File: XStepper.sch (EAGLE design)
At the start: 74 parts, among them Q2 16 MHZ

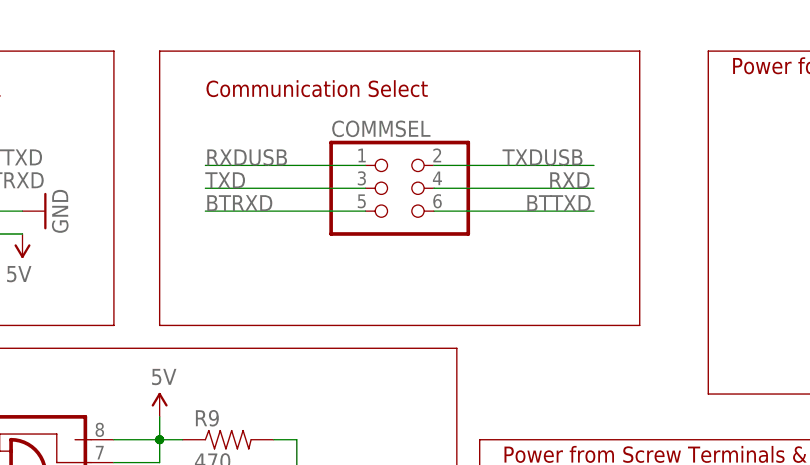
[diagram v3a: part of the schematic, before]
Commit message: - Bugfix COMSERIAL
change pins on comserial block
remove some unused files
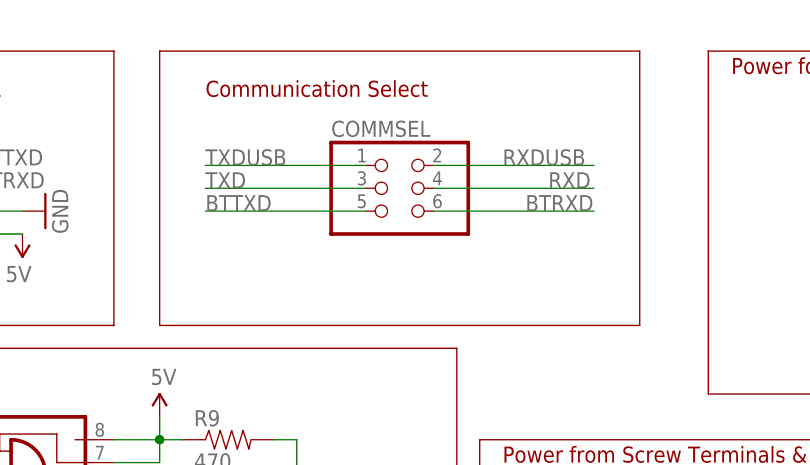
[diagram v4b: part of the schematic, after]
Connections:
- net BTRXD: now also COMMSEL.6; no longer COMMSEL.5
- net BTTXD: now also COMMSEL.5; no longer COMMSEL.6
- net RXDUSB: now also COMMSEL.2; no longer COMMSEL.1
- net TXDUSB: now also COMMSEL.1; no longer COMMSEL.2
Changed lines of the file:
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@@
 <grid distance="0.1" unitdist="inch" unit="inch" style="lines" multiple="1" display="no" altdistance="0.01" altunitdist="inch" altunit="inch"/>
 <layers>
-<layer number="1" name="Top" color="4" fill="1" visible="yes" active="no"/>
-<layer number="2" name="Route2" color="1" fill="3" visible="yes" active="no"/>
-<layer number="3" name="Route3" color="4" fill="3" visible="yes" active="no"/>
-<layer number="4" name="Route4" color="1" fill="4" visible="yes" active="no"/>
-<layer number="5" name="Route5" color="4" fill="4" visible="yes" active="no"/>
-<layer number="6" name="Route6" color="1" fill="8" visible="yes" active="no"/>
-<layer number="7" name="Route7" color="4" fill="8" visible="yes" active="no"/>
-<layer number="8" name="Route8" color="1" fill="2" visible="yes" active="no"/>
-<layer number="9" name="Route9" color="4" fill="2" visible="yes" active="no"/>
-<layer number="10" name="Route10" color="1" fill="7" visible="yes" active="no"/>
-<layer number="11" name="Route11" color="4" fill="7" visible="yes" active="no"/>
-<layer number="12" name="Route12" color="1" fill="5" visible="yes" active="no"/>
-<layer number="13" name="Route13" color="4" fill="5" visible="yes" active="no"/>
-<layer number="14" name="Route14" color="1" fill="6" visible="yes" active="no"/>
-<layer number="15" name="Route15" color="4" fill="6" visible="yes" active="no"/>
-<layer number="16" name="Bottom" color="1" fill="1" visible="yes" active="no"/>
-<layer number="17" name="Pads" color="2" fill="1" visible="yes" active="no"/>
-<layer number="18" name="Vias" color="2" fill="1" visible="yes" active="no"/>
-<layer number="19" name="Unrouted" color="6" fill="1" visible="yes" active="no"/>
-<layer number="20" name="Dimension" color="15" fill="1" visible="yes" active="no"/>
-<layer number="21" name="tPlace" color="7" fill="1" visible="yes" active="no"/>
-<layer number="22" name="bPlace" color="7" fill="1" visible="yes" active="no"/>
-<layer number="23" name="tOrigins" color="15" fill="1" visible="yes" active="no"/>
-<layer number="24" name="bOrigins" color="15" fill="1" visible="yes" active="no"/>
-<layer number="25" name="tNames" color="7" fill="1" visible="yes" active="no"/>
-<layer number="26" name="bNames" color="7" fill="1" visible="yes" active="no"/>
-<layer number="27" name="tValues" color="7" fill="1" visible="yes" active="no"/>
-<layer number="28" name="bValues" color="7" fill="1" visible="yes" active="no"/>
+<layer number="1" name="Top" color="4" fill="1" visible="no" active="no"/>
+<layer number="2" name="Route2" color="1" fill="3" visible="no" active="no"/>
+<layer number="3" name="Route3" color="4" fill="3" visible="no" active="no"/>
+<layer number="4" name="Route4" color="1" fill="4" visible="no" active="no"/>
+<layer number="5" name="Route5" color="4" fill="4" visible="no" active="no"/>
+<layer number="6" name="Route6" color="1" fill="8" visible="no" active="no"/>
+<layer number="7" name="Route7" color="4" fill="8" visible="no" active="no"/>
+<layer number="8" name="Route8" color="1" fill="2" visible="no" active="no"/>
+<layer number="9" name="Route9" color="4" fill="2" visible="no" active="no"/>
+<layer number="10" name="Route10" color="1" fill="7" visible="no" active="no"/>
+<layer number="11" name="Route11" color="4" fill="7" visible="no" active="no"/>
+<layer number="12" name="Route12" color="1" fill="5" visible="no" active="no"/>
+<layer number="13" name="Route13" color="4" fill="5" visible="no" active="no"/>
+<layer number="14" name="Route14" color="1" fill="6" visible="no" active="no"/>
+<layer number="15" name="Route15" color="4" fill="6" visible="no" active="no"/>
+<layer number="16" name="Bottom" color="1" fill="1" visible="no" active="no"/>
+<layer number="17" name="Pads" color="2" fill="1" visible="no" active="no"/>
+<layer number="18" name="Vias" color="2" fill="1" visible="no" active="no"/>
+<layer number="19" name="Unrouted" color="6" fill="1" visible="no" active="no"/>
+<layer number="20" name="Dimension" color="15" fill="1" visible="no" active="no"/>
+<layer number="21" name="tPlace" color="7" fill="1" visible="no" active="no"/>
+<layer number="22" name="bPlace" color="7" fill="1" visible="no" active="no"/>
+<layer number="23" name="tOrigins" color="15" fill="1" visible="no" active="no"/>
+<layer number="24" name="bOrigins" color="15" fill="1" visible="no" active="no"/>
+<layer number="25" name="tNames" color="7" fill="1" visible="no" active="no"/>
+<layer number="26" name="bNames" color="7" fill="1" visible="no" active="no"/>
+<layer number="27" name="tValues" color="7" fill="1" visible="no" active="no"/>
+<layer number="28" name="bValues" color="7" fill="1" visible="no" active="no"/>
 <layer number="29" name="tStop" color="7" fill="3" visible="no" active="no"/>
 <layer number="30" name="bStop" color="7" fill="6" visible="no" active="no"/>
@@
 <layer number="35" name="tGlue" color="7" fill="4" visible="no" active="no"/>
 <layer number="36" name="bGlue" color="7" fill="5" visible="no" active="no"/>
-<layer number="37" name="tTest" color="7" fill="1" visible="yes" active="no"/>
-<layer number="38" name="bTest" color="7" fill="1" visible="yes" active="no"/>
+<layer number="37" name="tTest" color="7" fill="1" visible="no" active="no"/>
+<layer number="38" name="bTest" color="7" fill="1" visible="no" active="no"/>
 <layer number="39" name="tKeepout" color="4" fill="11" visible="no" active="no"/>
 <layer number="40" name="bKeepout" color="1" fill="11" visible="no" active="no"/>
@@
 <layer number="44" name="Drills" color="7" fill="1" visible="no" active="no"/>
 <layer number="45" name="Holes" color="7" fill="1" visible="no" active="no"/>
-<layer number="46" name="Milling" color="3" fill="1" visible="yes" active="no"/>
-<layer number="47" name="Measures" color="7" fill="1" visible="yes" active="no"/>
-<layer number="48" name="Document" color="7" fill="1" visible="yes" active="no"/>
-<layer number="49" name="Reference" color="7" fill="1" visible="yes" active="no"/>
-<layer number="50" name="dxf" color="7" fill="1" visible="yes" active="no"/>
-<layer number="51" name="tDocu" color="7" fill="1" visible="yes" active="no"/>
-<layer number="52" name="bDocu" color="7" fill="1" visible="yes" active="no"/>
-<layer number="53" name="tGND_GNDA" color="7" fill="9" visible="yes" active="no"/>
-<layer number="54" name="bGND_GNDA" color="1" fill="9" visible="yes" active="no"/>
-<layer number="56" name="wert" color="7" fill="1" visible="yes" active="no"/>
+<layer number="46" name="Milling" color="3" fill="1" visible="no" active="no"/>
+<layer number="47" name="Measures" color="7" fill="1" visible="no" active="no"/>
+<layer number="48" name="Document" color="7" fill="1" visible="no" active="no"/>
+<layer number="49" name="Reference" color="7" fill="1" visible="no" active="no"/>
+<layer number="50" name="dxf" color="7" fill="1" visible="no" active="no"/>
+<layer number="51" name="tDocu" color="7" fill="1" visible="no" active="no"/>
+<layer number="52" name="bDocu" color="7" fill="1" visible="no" active="no"/>
+<layer number="53" name="tGND_GNDA" color="7" fill="9" visible="no" active="no"/>
+<layer number="54" name="bGND_GNDA" color="1" fill="9" visible="no" active="no"/>
+<layer number="56" name="wert" color="7" fill="1" visible="no" active="no"/>
 <layer number="91" name="Nets" color="2" fill="1" visible="yes" active="yes"/>
 <layer number="92" name="Busses" color="1" fill="1" visible="yes" active="yes"/>
@@
 </segment>
 <segment>
+<pinref part="COMMSEL" gate="A" pin="5"/>
+<wire x1="101.6" y1="162.56" x2="83.82" y2="162.56" width="0.1524" layer="91"/>
+<label x="83.82" y="162.56" size="1.778" layer="95"/>
+</segment>
+</net>
+<net name="BTRXD" class="0">
+<segment>
+<pinref part="BT-TTL" gate="A" pin="3"/>
+<wire x1="50.8" y1="165.1" x2="58.42" y2="165.1" width="0.1524" layer="91"/>
+<label x="58.42" y="165.1" size="1.778" layer="95"/>
+</segment>
+<segment>
 <pinref part="COMMSEL" gate="A" pin="6"/>
 <wire x1="109.22" y1="162.56" x2="127" y2="162.56" width="0.1524" layer="91"/>
@@
 </segment>
 </net>
-<net name="BTRXD" class="0">
-<segment>
-<pinref part="BT-TTL" gate="A" pin="3"/>
-<wire x1="50.8" y1="165.1" x2="58.42" y2="165.1" width="0.1524" layer="91"/>
-<label x="58.42" y="165.1" size="1.778" layer="95"/>
-</segment>
-<segment>
-<pinref part="COMMSEL" gate="A" pin="5"/>
-<wire x1="101.6" y1="162.56" x2="83.82" y2="162.56" width="0.1524" layer="91"/>
-<label x="83.82" y="162.56" size="1.778" layer="95"/>
-</segment>
-</net>
 <net name="TXDUSB" class="0">
 <segment>
@@
 </segment>
 <segment>
-<pinref part="COMMSEL" gate="A" pin="2"/>
-<wire x1="109.22" y1="167.64" x2="127" y2="167.64" width="0.1524" layer="91"/>
-<label x="116.84" y="167.64" size="1.778" layer="95"/>
+<pinref part="COMMSEL" gate="A" pin="1"/>
+<wire x1="101.6" y1="167.64" x2="83.82" y2="167.64" width="0.1524" layer="91"/>
+<label x="83.82" y="167.64" size="1.778" layer="95"/>
 </segment>
 </net>
@@
 </segment>
 <segment>
-<pinref part="COMMSEL" gate="A" pin="1"/>
-<wire x1="101.6" y1="167.64" x2="83.82" y2="167.64" width="0.1524" layer="91"/>
-<label x="83.82" y="167.64" size="1.778" layer="95"/>
-</segment>
-</net>
+<pinref part="COMMSEL" gate="A" pin="2"/>
+<wire x1="109.22" y1="167.64" x2="127" y2="167.64" width="0.1524" layer="91"/>
+<label x="116.84" y="167.64" size="1.778" layer="95"/>
+</segment>
+</net>

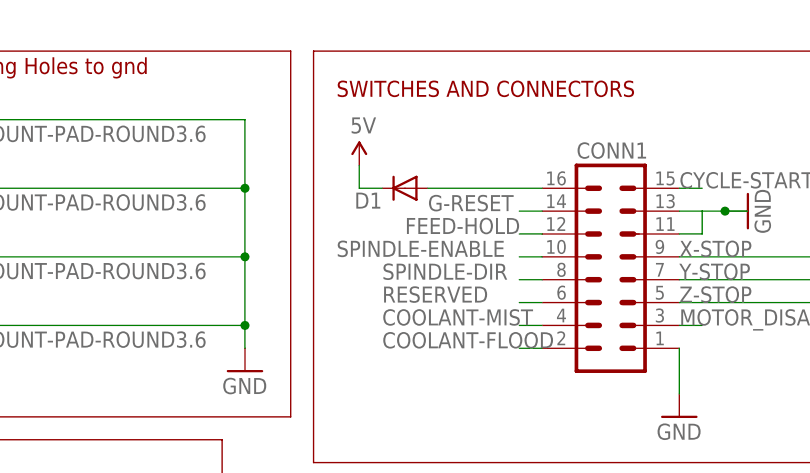
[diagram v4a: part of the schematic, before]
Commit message: - bugfix diode
- add new autorouting
- move emergency screw near to cpu
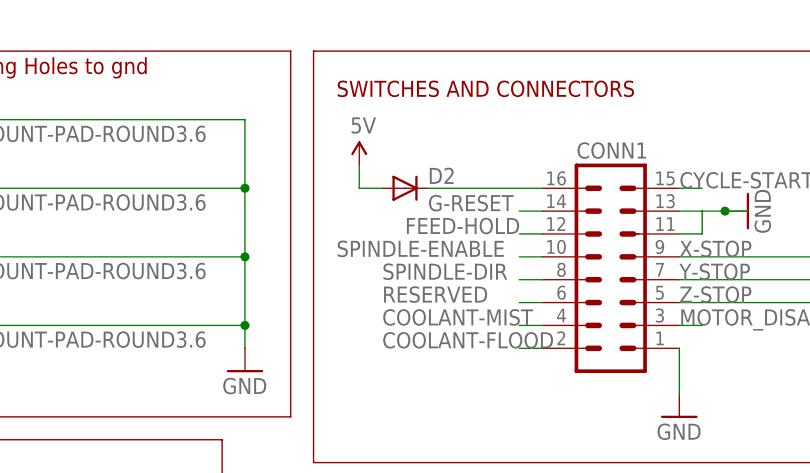
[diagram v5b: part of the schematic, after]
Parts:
- renumbered D1 to D2
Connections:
- net 5V: now also D2.A; no longer D2.C
- net N$45: now also D2.C; no longer D2.A
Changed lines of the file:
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@@
 </variantdefs>
 <classes>
-<class number="0" name="default" width="0.4064" drill="0">
-<clearance class="0" value="0.254"/>
+<class number="0" name="default" width="0.3048" drill="0">
+<clearance class="0" value="0.2032"/>
 </class>
 <class number="1" name="power" width="1.016" drill="0">
@@
 <part name="R13" library="SparkFun-Resistors" deviceset="RESISTOR" device="AXIAL-0.3"/>
 <part name="R14" library="SparkFun-Resistors" deviceset="RESISTOR" device="AXIAL-0.3"/>
-<part name="D1" library="SparkFun-DiscreteSemi" deviceset="DIODE" device="PTH"/>
 <part name="&lt;ESTOP" library="con-ptr500" deviceset="AK500/2" device=""/>
 <part name="GND39" library="SparkFun" deviceset="GND" device=""/>
@@
 <part name="GND" library="jumper" deviceset="JP1E" device=""/>
 <part name="GND21" library="SparkFun" deviceset="GND" device=""/>
+<part name="D2" library="SparkFun-DiscreteSemi" deviceset="DIODE" device="PTH"/>
 </parts>
 <sheets>
@@
 <instance part="R13" gate="G$1" x="332.74" y="165.1" rot="R270"/>
 <instance part="R14" gate="G$1" x="340.36" y="165.1" rot="R270"/>
-<instance part="D1" gate="G$1" x="236.22" y="165.1" rot="R180"/>
 <instance part="&lt;ESTOP" gate="-1" x="15.24" y="0"/>
 <instance part="&lt;ESTOP" gate="-2" x="15.24" y="-7.62"/>
@@
 <instance part="GND" gate="A" x="22.86" y="121.92" rot="R90"/>
 <instance part="GND21" gate="1" x="30.48" y="124.46" rot="R90"/>
+<instance part="D2" gate="G$1" x="236.22" y="165.1"/>
 </instances>
 <busses>
@@
 </segment>
 <segment>
-<pinref part="D1" gate="G$1" pin="C"/>
 <pinref part="U$16" gate="G$1" pin="5V"/>
 <wire x1="233.68" y1="165.1" x2="231.14" y2="165.1" width="0.1524" layer="91"/>
 <wire x1="231.14" y1="165.1" x2="231.14" y2="167.64" width="0.1524" layer="91"/>
+<pinref part="D2" gate="G$1" pin="A"/>
 </segment>
 </net>
@@
 </segment>
 </net>
-<net name="PWRMOT" class="0">
+<net name="PWRMOT" class="1">
 <segment>
 <pinref part="MOT" gate="-1" pin="KL"/>
@@
 <segment>
 <pinref part="CONN1" gate="1" pin="16"/>
-<pinref part="D1" gate="G$1" pin="A"/>
 <wire x1="251.46" y1="165.1" x2="238.76" y2="165.1" width="0.1524" layer="91"/>
-</segment>
-</net>
+<pinref part="D2" gate="G$1" pin="C"/>
+</segment>
+</net>
